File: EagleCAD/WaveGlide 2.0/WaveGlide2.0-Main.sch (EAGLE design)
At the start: 27 parts, among them CN3 0, K2 MS-20-310-HN, Q2 reset, U1 ATMEGA328P_TQFP, U2 BMP180, U3 MPXV7002, U5 UG-2828GDEDF11, Y2 12MHz

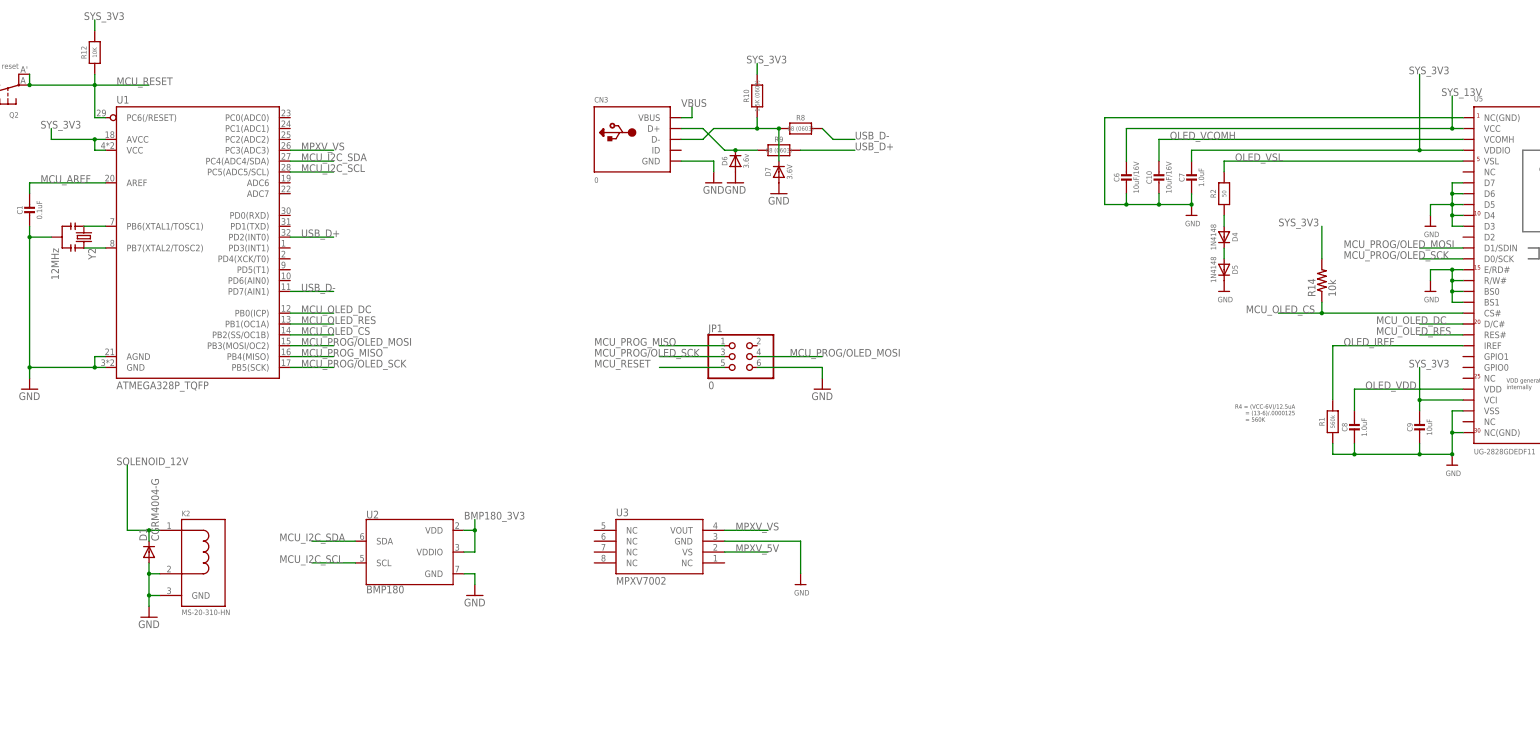
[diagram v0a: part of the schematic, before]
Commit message: Add buffer divider network, and floorplanning
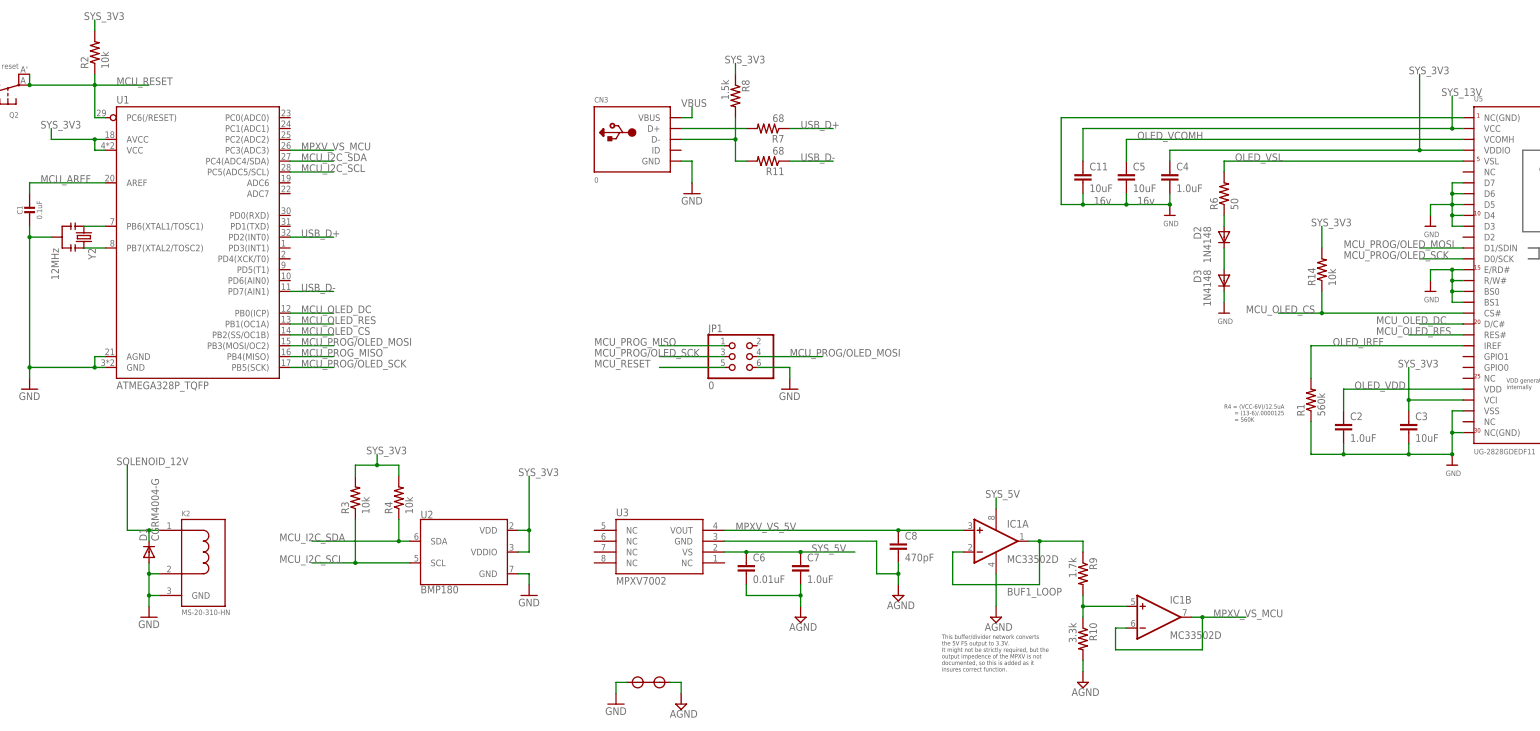
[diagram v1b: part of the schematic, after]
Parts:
- removed C10: 10uF/16V, microbuilder:CAP_CERAMIC_0805MP
- removed C9: 10uF, microbuilder:CAP_CERAMIC_0805MP
- removed D4, D5: 1N4148, microbuilder:DIODESOD-323
- removed D6: 3.6v, microbuilder:DIODESOD-323
- removed D7: 3.6V, microbuilder:DIODESOD-323
- removed R12: 10K, microbuilder:RESISTOR0805_NOOUTLINE
- added C11, C3, C5: 10uF, resistor:C-EUC0805
- added C2, C4: 1.0uF, resistor:C-EUC0805
- added D2, D3: 1N4148, diode:DIODE-SOD323-W
- added IC1: MC33502D, linear:MC33078D
- added R11, R7: 68, resistor:R-US_R0603
- added R3, R4: 10k, resistor:R-US_R0603
- added R6: 50, resistor:R-US_R0603
- added U$2: SHORT, CustomParts:SHORT
- C6: value 10uF/16V -> 0.01uF; device microbuilder:CAP_CERAMIC_0805MP -> resistor:C-EUC0805
- C7: device microbuilder:CAP_CERAMIC_0805MP -> resistor:C-EUC0805
- C8: value 1.0uF -> 470pF; device microbuilder:CAP_CERAMIC_0805MP -> resistor:C-EUC0805
- R1: device microbuilder:RESISTOR_0805MP -> resistor:R-US_R0603
- R10: value 1.5K (0603) -> 3.3k; device microbuilder:RESISTOR_0603_NOOUT -> resistor:R-US_R0603; TOLLERANCE (none) -> 1%
- R2: value 50 -> 10k; device microbuilder:RESISTOR_0805MP -> resistor:R-US_R0603
- R8: value 68 (0603) -> 1.5k; device microbuilder:RESISTOR_0603_NOOUT -> resistor:R-US_R0603
- R9: value 68 (0603) -> 1.7k; device microbuilder:RESISTOR_0603_NOOUT -> resistor:R-US_R0603; TOLLERANCE (none) -> 1%
- U1: device CustomParts:ATMEGA328P_TQFP -> CustomParts:ATMEGA328P_TQFP32
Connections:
- removed net BMP180_3V3: U2.VDD, U2.VDDIO
- removed net MPXV_5V: U3.VS
- removed net MPXV_VS: U1.PC3(ADC3), U3.VOUT
- removed net N$5: D4.C, D5.A
- new net AGND: C6.2, C7.2, C8.2, IC1P.V-, R10.2, U$2.P$2, U3.GND
- new net BUF1_LOOP: IC1A.-IN, IC1A.OUT, R9.1
- new net MPXV_VS_5V: C8.1, IC1A.+IN, U3.VOUT
- new net MPXV_VS_MCU: IC1B.-IN, IC1B.OUT, U1.PC3(ADC3)
- new net N$1: D2.C, D3.A
- new net N$4: IC1B.+IN, R10.1, R9.2
- new net SYS_5V: C6.1, C7.1, IC1P.V+, U3.VS
- net D+1: now also R7.2; no longer D6.C, R9.1
- net D-1: now also R11.2, R8.2; no longer D7.C, R10.1, R8.1
- net GND: now also C11.2, C2.2, C3.2, C4.2, C5.2, D3.C, U$2.P$1; no longer C10.2, C6.2, C7.2, C8.2, C9.2, D5.C, D6.A, D7.A, U3.GND
- net MCU_I2C_SCL: now also R3.1
- net MCU_I2C_SDA: now also R4.1
- net MCU_RESET: now also R2.1; no longer R12.1
- net N$2: now also D2.A, R6.1; no longer D4.A, R2.1
- net OLED_VCOMH: now also C5.1; no longer C10.1
- net OLED_VDD: now also C2.1; no longer C8.1
- net OLED_VSL: now also R6.2; no longer R2.2
- net SYS_13V: now also C11.1; no longer C6.1
- net SYS_3V3: now also C3.1, C4.1, R2.2, R3.2, R4.2, R8.1, U2.VDD, U2.VDDIO; no longer C7.1, C9.1, R10.2, R12.2
- net USB_D+: now also R7.1; no longer R9.2
- net USB_D-: now also R11.1; no longer R8.2
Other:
- note added: "This buffer/divider network converts the 5V FS output to 3.3V. It might not be strictly required, but the output impedence of the MPXV is not documented, so this is added as it insures correct function."
- moved on the sheet: C6, C7, C8, R14, U2

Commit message: Add TPS55340 boost circuit
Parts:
- added C10, C16: 100nF, resistor:C-EUC0805
- added C12: 22nF, resistor:C-EUC0805
- added C13: 10nF, resistor:C-EUC0805
- added C14: 22uF, resistor:C-EUC1210
- added C15: 1.0uF, resistor:C-EUC0805
- added C9: 10uF, resistor:C-EUC0805
- added L1: 3.3uH, resistor:L-USL4532P
- added R12: 953, resistor:R-US_R0603
- added R13: 86.6k, resistor:R-US_R0603
- added R15: 10k, resistor:R-US_R0603
- added R5: 60.4k, resistor:R-US_R0603
- added U4: TPS55340PWP, CustomParts:TPS55340PWP
- C1: device microbuilder:CAP_CERAMIC_0805MP -> resistor:C-EUC0805; POPULATE (none) -> 1
- C11, C5: POPULATE (none) -> 1; VOLT (none) -> 16V; VOLTAGE 16v -> (none)
- C2, C3, C4, C6, C7, C8, CN3, D1, D3, IC1, JP1, K2, Q2, R1, R11, R14, R2, R3, R4, R6, R7, R8, U$2, U2, U3, U5, Y2: POPULATE (none) -> 1
- D2: MPN (none) -> MBRD835LT4G; POPULATE (none) -> 1
- R10, R9: POPULATE (none) -> 1; TOL (none) -> 1%; TOLLERANCE 1% -> (none)
- U1: MPN (none) -> TPS55340RTER; POPULATE (none) -> 1
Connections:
- new net SOLENOID_EN: U4.EN
- new net TPS55340_COMP: C13.1, R12.2, U4.COMP
- new net TPS55340_FB: R13.2, R15.1, U4.FB
- new net TPS55340_FREQ: R5.2, U4.FREQ
- new net TPS55340_SS: C12.1, U4.SS
- new net TPS55340_SW: L1.1, U4.SW@1, U4.SW@2
- new net TPS66340_COMP1: C16.1, R12.1
- new net VBAT: C10.1, C9.1, L1.2, U4.VIN
- net GND: now also C10.2, C12.2, C13.2, C14.2, C15.2, C16.2, C9.2, R15.2, R5.1, U4.AGND, U4.EPAD, U4.PGND@1, U4.PGND@2, U4.PGND@3
- net SOLENOID_12V: now also C14.1, C15.1, R13.1
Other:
- note added: "DIODE GOES HERE"
